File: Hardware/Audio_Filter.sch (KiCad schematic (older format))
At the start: 20 parts, among them U12 NE5534, U13 NE5534, U14 NE5534

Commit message: Currently adding level shifters
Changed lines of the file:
@@
 LIBS:microchip_pic18mcu
 LIBS:microchip
+LIBS:microchip1
 LIBS:microcontrollers
 LIBS:motorola
@@
 LIBS:sensors
 LIBS:siliconi
+LIBS:special
 LIBS:stm8
 LIBS:stm32
@@
 $Descr A4 11693 8268
 encoding utf-8
-Sheet 3 8
+Sheet 2 8
 Title "Audio Filter"
 Date ""
@@
 AR Path="/57B136AF/57B0E099" Ref="#PWR140"  Part="1"
 AR Path="/57B0BDCC/57B0E099" Ref="#PWR150"  Part="1"
-F 0 "#PWR150" H 3150 3450 30  0001 C CNN
+F 0 "#PWR140" H 3150 3450 30  0001 C CNN
 F 1 "GND" H 3150 3380 30  0001 C CNN
 F 2 "" H 3150 3450 60  0000 C CNN
@@
 AR Path="/57B136AF/57B0E0AF" Ref="C54"  Part="1"
 AR Path="/57B0BDCC/57B0E0AF" Ref="C62"  Part="1"
-F 0 "C62" V 3750 2300 40  0000 L CNN
+F 0 "C54" V 3750 2300 40  0000 L CNN
 F 1 "2700pF" V 3750 1900 40  0000 L CNN
 F 2 "" H 3738 2050 30  0000 C CNN
@@
 AR Path="/57B136AF/57B0E0B6" Ref="R58"  Part="1"
 AR Path="/57B0BDCC/57B0E0B6" Ref="R67"  Part="1"
-F 0 "R67" V 3780 2400 40  0000 C CNN
+F 0 "R58" V 3780 2400 40  0000 C CNN
 F 1 "820" V 3707 2401 40  0000 C CNN
 F 2 "" V 3630 2400 30  0000 C CNN
@@
 	3100 2200 3100 3100
 Wire Wire Line
-	3100 2400 3450 2400
+	3100 2400 3550 2400
 Connection ~ 3100 3100
 Wire Wire Line
-	3100 2200 3500 2200
+	3100 2200 3550 2200
 Connection ~ 3100 2400
 Wire Wire Line
@@
 	4300 2200 4300 3200
 Wire Wire Line
-	4300 2400 3950 2400
+	3850 2400 4300 2400
 Connection ~ 4300 3200
 Wire Wire Line
-	3900 2200 4300 2200
+	3850 2200 4300 2200
 Connection ~ 4300 2400
 $Comp
@@
 AR Path="/57B136AF/57B0E0C8" Ref="C55"  Part="1"
 AR Path="/57B0BDCC/57B0E0C8" Ref="C63"  Part="1"
-F 0 "C63" V 4000 2700 40  0000 L CNN
+F 0 "C55" V 4000 2700 40  0000 L CNN
 F 1 "22pF" V 4000 2400 40  0000 L CNN
 F 2 "" H 3988 2450 30  0000 C CNN
@@
 AR Path="/57B136AF/57B0E0D2" Ref="#PWR141"  Part="1"
 AR Path="/57B0BDCC/57B0E0D2" Ref="#PWR151"  Part="1"
-F 0 "#PWR151" H 3150 5500 30  0001 C CNN
+F 0 "#PWR141" H 3150 5500 30  0001 C CNN
 F 1 "GND" H 3150 5430 30  0001 C CNN
 F 2 "" H 3150 5500 60  0000 C CNN
@@
 AR Path="/57B136AF/57B0E0E8" Ref="C58"  Part="1"
 AR Path="/57B0BDCC/57B0E0E8" Ref="C66"  Part="1"
-F 0 "C66" V 3750 4350 40  0000 L CNN
+F 0 "C58" V 3750 4350 40  0000 L CNN
 F 1 "2700pF" V 3750 3950 40  0000 L CNN
 F 2 "" H 3738 4100 30  0000 C CNN
@@
 AR Path="/57B136AF/57B0E0EF" Ref="R65"  Part="1"
 AR Path="/57B0BDCC/57B0E0EF" Ref="R74"  Part="1"
-F 0 "R74" V 3780 4450 40  0000 C CNN
+F 0 "R65" V 3780 4450 40  0000 C CNN
 F 1 "820" V 3707 4451 40  0000 C CNN
 F 2 "" V 3630 4450 30  0000 C CNN
@@
 	3100 4250 3100 5150
 Wire Wire Line
-	3100 4450 3450 4450
+	3100 4450 3550 4450
 Connection ~ 3100 5150
 Wire Wire Line
-	3100 4250 3500 4250
+	3100 4250 3550 4250
 Connection ~ 3100 4450
 Wire Wire Line
@@
 	4300 4250 4300 5250
 Wire Wire Line
-	4300 4450 3950 4450
+	3850 4450 4300 4450
 Connection ~ 4300 5250
 Wire Wire Line
-	3900 4250 4300 4250
+	3850 4250 4300 4250
 Connection ~ 4300 4450
 $Comp
@@
 AR Path="/57B136AF/57B0E101" Ref="R63"  Part="1"
 AR Path="/57B0BDCC/57B0E101" Ref="R72"  Part="1"
-F 0 "R72" V 4930 4350 40  0000 C CNN
+F 0 "R63" V 4930 4350 40  0000 C CNN
 F 1 "220" V 4857 4351 40  0000 C CNN
 F 2 "" V 4780 4350 30  0000 C CNN
@@
 AR Path="/57B136AF/57B0E108" Ref="R60"  Part="1"
 AR Path="/57B0BDCC/57B0E108" Ref="R69"  Part="1"
-F 0 "R69" V 4930 4150 40  0000 C CNN
+F 0 "R60" V 4930 4150 40  0000 C CNN
 F 1 "220" V 4857 4151 40  0000 C CNN
 F 2 "" V 4780 4150 30  0000 C CNN
@@
 	4500 5250 4500 4350
 Wire Wire Line
-	4500 4350 4600 4350
+	4500 4350 4700 4350
 Wire Wire Line
 	4500 3200 4500 4150
 Wire Wire Line
-	4500 4150 4600 4150
-Wire Wire Line
-	5100 4350 5900 4350
-Wire Wire Line
-	5100 4150 5900 4150
+	4500 4150 4700 4150
+Wire Wire Line
+	5000 4350 6000 4350
+Wire Wire Line
+	5000 4150 6000 4150
 $Comp
 L C-RESCUE-museV2 C59
@@
 AR Path="/57B136AF/57B0E115" Ref="C59"  Part="1"
 AR Path="/57B0BDCC/57B0E115" Ref="C67"  Part="1"
-F 0 "C67" V 5500 4350 40  0000 L CNN
+F 0 "C59" V 5500 4350 40  0000 L CNN
 F 1 "27000pF" V 5400 3900 40  0000 L CNN
 F 2 "" H 5488 4100 30  0000 C CNN
@@
 $EndComp
 Wire Wire Line
-	5250 4250 5200 4250
+	5200 4250 5300 4250
 Wire Wire Line
 	5200 4250 5200 4350
 Connection ~ 5200 4350
 Wire Wire Line
-	5650 4250 5700 4250
+	5600 4250 5700 4250
 Wire Wire Line
 	5700 4250 5700 4150
@@
 AR Path="/57B136AF/57B0E122" Ref="R61"  Part="1"
 AR Path="/57B0BDCC/57B0E122" Ref="R70"  Part="1"
-F 0 "R70" V 6230 4150 40  0000 C CNN
+F 0 "R61" V 6230 4150 40  0000 C CNN
 F 1 "180" V 6157 4151 40  0000 C CNN
 F 2 "" V 6080 4150 30  0000 C CNN
@@
 AR Path="/57B136AF/57B0E129" Ref="R64"  Part="1"
 AR Path="/57B0BDCC/57B0E129" Ref="R73"  Part="1"
-F 0 "R73" V 6230 4350 40  0000 C CNN
+F 0 "R64" V 6230 4350 40  0000 C CNN
 F 1 "180" V 6157 4351 40  0000 C CNN
 F 2 "" V 6080 4350 30  0000 C CNN
@@
 $EndComp
 Wire Wire Line
-	6400 4350 6600 4350
-Wire Wire Line
-	6400 4150 6600 4150
+	6300 4350 6600 4350
+Wire Wire Line
+	6300 4150 6600 4150
 $Comp
 L GND-RESCUE-museV2 #PWR146
@@
 AR Path="/57B136AF/57B0E132" Ref="#PWR146"  Part="1"
 AR Path="/57B0BDCC/57B0E132" Ref="#PWR156"  Part="1"
-F 0 "#PWR156" H 5850 5050 30  0001 C CNN
+F 0 "#PWR146" H 5850 5050 30  0001 C CNN
 F 1 "GND" H 5850 4980 30  0001 C CNN
 F 2 "" H 5850 5050 60  0000 C CNN
@@
 AR Path="/57B136AF/57B0E13A" Ref="R66"  Part="1"
 AR Path="/57B0BDCC/57B0E13A" Ref="R75"  Part="1"
-F 0 "R75" V 5930 4700 40  0000 C CNN
+F 0 "R66" V 5930 4700 40  0000 C CNN
 F 1 "200" V 5857 4701 40  0000 C CNN
 F 2 "" V 5780 4700 30  0000 C CNN
@@
 $EndComp
 Wire Wire Line
-	5850 5050 5850 4950
-Wire Wire Line
-	5850 4350 5850 4450
+	5850 4850 5850 5050
+Wire Wire Line
+	5850 4350 5850 4550
 $Comp
 L R-RESCUE-museV2 R59
@@
 AR Path="/57B136AF/57B0E143" Ref="R59"  Part="1"
 AR Path="/57B0BDCC/57B0E143" Ref="R68"  Part="1"
-F 0 "R68" V 5930 3800 40  0000 C CNN
+F 0 "R59" V 5930 3800 40  0000 C CNN
 F 1 "200" V 5857 3801 40  0000 C CNN
 F 2 "" V 5780 3800 30  0000 C CNN
@@
 $EndComp
 Wire Wire Line
-	5850 4050 5850 4150
+	5850 3950 5850 4150
 Connection ~ 5850 4150
 $Comp
@@
 AR Path="/57B136AF/57B0E14C" Ref="C57"  Part="1"
 AR Path="/57B0BDCC/57B0E14C" Ref="C65"  Part="1"
-F 0 "C65" H 6500 3900 40  0000 L CNN
+F 0 "C57" H 6500 3900 40  0000 L CNN
 F 1 "8200pF" H 6506 3715 40  0000 L CNN
 F 2 "" H 6538 3650 30  0000 C CNN
@@
 $EndComp
 Wire Wire Line
-	6500 4000 6500 4150
+	6500 3950 6500 4150
 Connection ~ 6500 4150
 $Comp
@@
 AR Path="/57B136AF/57B0E155" Ref="C61"  Part="1"
 AR Path="/57B0BDCC/57B0E155" Ref="C69"  Part="1"
-F 0 "C69" H 6500 4800 40  0000 L CNN
+F 0 "C61" H 6500 4800 40  0000 L CNN
 F 1 "8200pF" H 6506 4615 40  0000 L CNN
 F 2 "" H 6538 4550 30  0000 C CNN
@@
 $EndComp
 Wire Wire Line
-	6500 4350 6500 4500
+	6500 4350 6500 4550
 Connection ~ 6500 4350
 $Comp
@@
 AR Path="/57B136AF/57B0E15E" Ref="#PWR147"  Part="1"
 AR Path="/57B0BDCC/57B0E15E" Ref="#PWR157"  Part="1"
-F 0 "#PWR157" H 6500 5050 30  0001 C CNN
+F 0 "#PWR147" H 6500 5050 30  0001 C CNN
 F 1 "GND" H 6500 4980 30  0001 C CNN
 F 2 "" H 6500 5050 60  0000 C CNN
@@
 $EndComp
 Wire Wire Line
-	6500 5050 6500 4900
+	6500 4850 6500 5050
 $Comp
 L NE5534 U12
@@
 AR Path="/57B136AF/57B0E165" Ref="U12"  Part="1"
 AR Path="/57B0BDCC/57B0E165" Ref="U15"  Part="1"
-F 0 "U15" H 3850 3350 60  0000 C CNN
+F 0 "U12" H 3850 3350 60  0000 C CNN
 F 1 "NE5534" H 3850 3450 60  0000 C CNN
 F 2 "" H 3700 3200 60  0000 C CNN
@@
 $EndComp
 Wire Wire Line
-	3750 2600 3700 2600
+	3700 2600 3800 2600
 Wire Wire Line
 	3700 2600 3700 2800
@@
 	4200 2750 4200 2600
 Wire Wire Line
-	4200 2600 4150 2600
+	4200 2600 4100 2600
 $Comp
 L C-RESCUE-museV2 C60
@@
 AR Path="/57B136AF/57B0E172" Ref="C60"  Part="1"
 AR Path="/57B0BDCC/57B0E172" Ref="C68"  Part="1"
-F 0 "C68" V 4000 4750 40  0000 L CNN
+F 0 "C60" V 4000 4750 40  0000 L CNN
 F 1 "22pF" V 4000 4450 40  0000 L CNN
 F 2 "" H 3988 4500 30  0000 C CNN
@@
 AR Path="/57B136AF/57B0E179" Ref="U14"  Part="1"
 AR Path="/57B0BDCC/57B0E179" Ref="U17"  Part="1"
-F 0 "U17" H 3850 5400 60  0000 C CNN
+F 0 "U14" H 3850 5400 60  0000 C CNN
 F 1 "NE5534" H 3850 5500 60  0000 C CNN
 F 2 "" H 3700 5250 60  0000 C CNN
@@
 $EndComp
 Wire Wire Line
-	3750 4650 3700 4650
+	3700 4650 3800 4650
 Wire Wire Line
 	3700 4650 3700 4850
@@
 	4200 4800 4200 4650
 Wire Wire Line
-	4200 4650 4150 4650
+	4200 4650 4100 4650
 $Comp
 L NE5534 U13
@@
 AR Path="/57B136AF/57B0E186" Ref="U13"  Part="1"
 AR Path="/57B0BDCC/57B0E186" Ref="U16"  Part="1"
-F 0 "U16" H 7250 4400 60  0000 C CNN
+F 0 "U13" H 7250 4400 60  0000 C CNN
 F 1 "NE5534" H 7250 4500 60  0000 C CNN
 F 2 "" H 7100 4250 60  0000 C CNN
@@
 AR Path="/57B136AF/57B0E19A" Ref="C56"  Part="1"
 AR Path="/57B0BDCC/57B0E19A" Ref="C64"  Part="1"
-F 0 "C64" V 7400 3750 40  0000 L CNN
+F 0 "C56" V 7400 3750 40  0000 L CNN
 F 1 "22pF" V 7400 3450 40  0000 L CNN
 F 2 "" H 7388 3500 30  0000 C CNN
@@
 $EndComp
 Wire Wire Line
-	7150 3650 7100 3650
+	7100 3650 7200 3650
 Wire Wire Line
 	7100 3650 7100 3850
@@
 	7600 3800 7600 3650
 Wire Wire Line
-	7600 3650 7550 3650
-Wire Wire Line
-	5850 3550 5850 3450
+	7600 3650 7500 3650
+Wire Wire Line
+	5850 3450 5850 3650
 Wire Wire Line
 	5850 3450 7700 3450
@@
 	7700 3450 7700 4250
 Wire Wire Line
-	7600 4250 7800 4250
-Wire Wire Line
-	6500 3600 6500 3450
+	7600 4250 7900 4250
+Wire Wire Line
+	6500 3450 6500 3650
 Connection ~ 6500 3450
 $Comp
@@
 AR Path="/57B136AF/57B0E1AD" Ref="R62"  Part="1"
 AR Path="/57B0BDCC/57B0E1AD" Ref="R71"  Part="1"
-F 0 "R71" V 8130 4250 40  0000 C CNN
+F 0 "R62" V 8130 4250 40  0000 C CNN
 F 1 "100" V 8057 4251 40  0000 C CNN
 F 2 "" V 7980 4250 30  0000 C CNN
@@
 ANALOG_OUT
 Wire Wire Line
-	8400 4250 8300 4250
+	8200 4250 8400 4250
 $Comp
 L -15VSB #PWR?

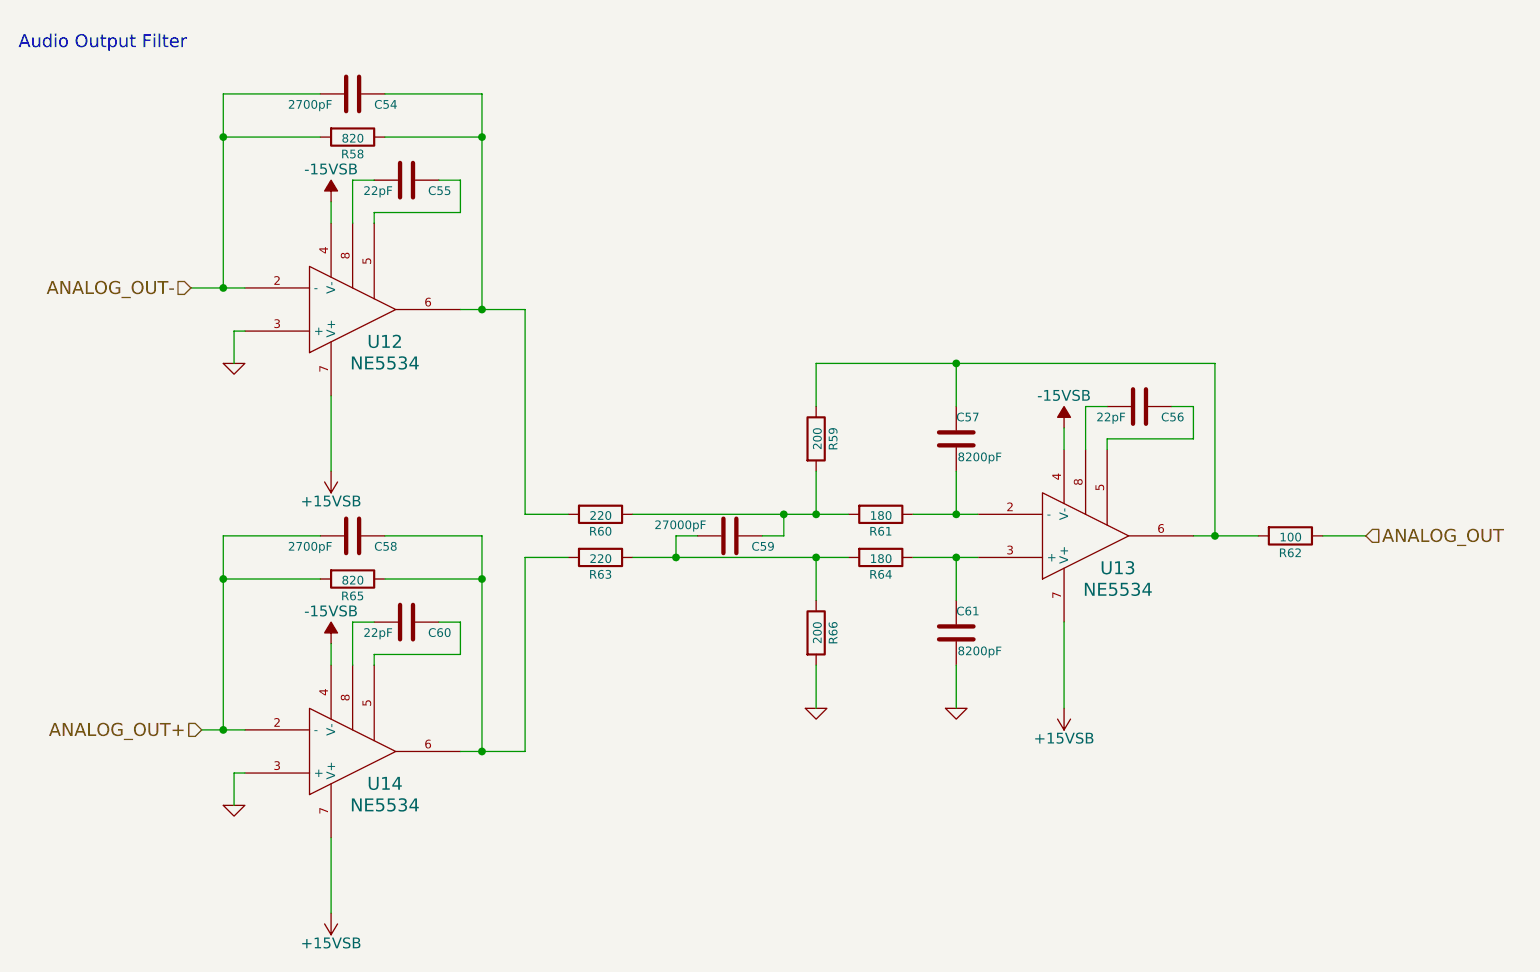
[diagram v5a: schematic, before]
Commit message: Changing to global labels/pages in progress
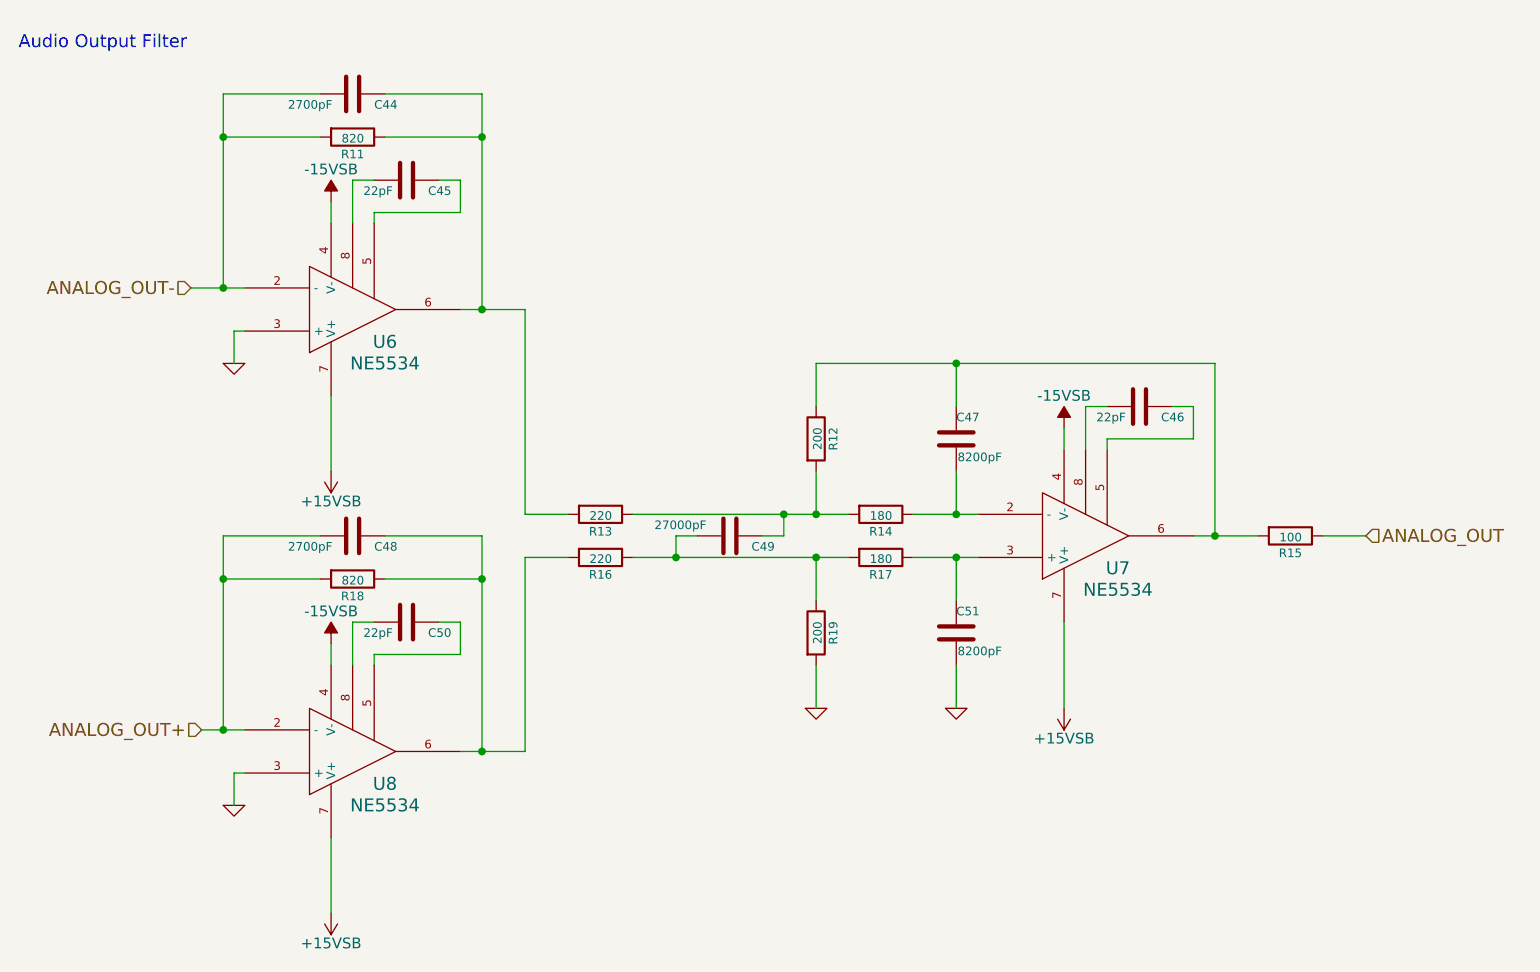
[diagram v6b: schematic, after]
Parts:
- renumbered C54 to C36, C55 to C37, C56 to C38, C57 to C39, C58 to C40, C59 to C41, C60 to C42, C61 to C43, R66 to R10, R58 to R2, R59 to R3, R60 to R4, R61 to R5, R62 to R6, R63 to R7, R64 to R8, R65 to R9, U12 to U3, U13 to U4, U14 to U5

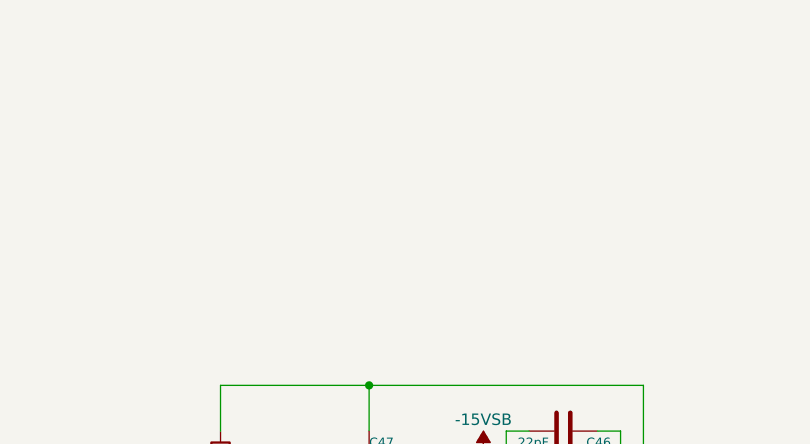
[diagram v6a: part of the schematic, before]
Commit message: Finished converting to global labels
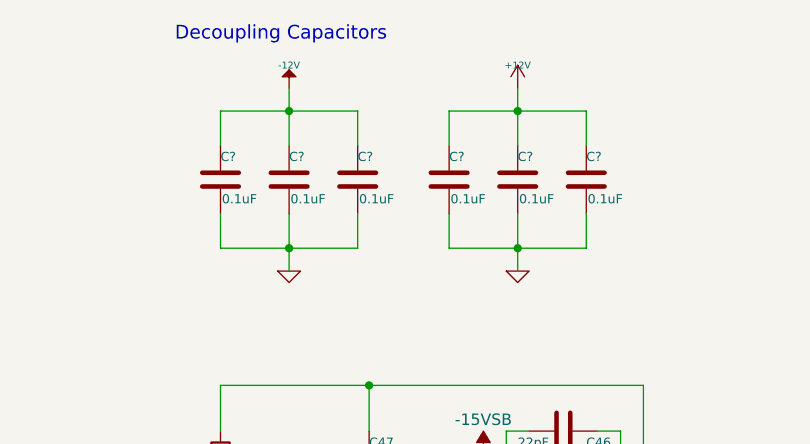
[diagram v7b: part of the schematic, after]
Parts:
- added C? (x6): 0.1uF, symbol C-RESCUE-museV2
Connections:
- net GND: now also C?.2, C?.2, C?.2, C?.2, C?.2, C?.2
- new net +12V: C?.1, C?.1, C?.1
- new net -12V: C?.1, C?.1, C?.1
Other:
- note added: "Decoupling Capacitors"
